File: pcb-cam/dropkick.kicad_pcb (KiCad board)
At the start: 2 copper layers, 44.5 x 50.8 mm, 55 parts, among them J1 Conn_01x10, SW1 450405020524, SW2 KMR211NG_LFS, U1 SPX3819-3.3, U2 MCP73831T-2ACI/OT, U3 CAM-M8C-0, U4 ATSAMD21G18A-AUT, U5 DPS310XTSA1, U6 MPU-6050, X1 USB micro-B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

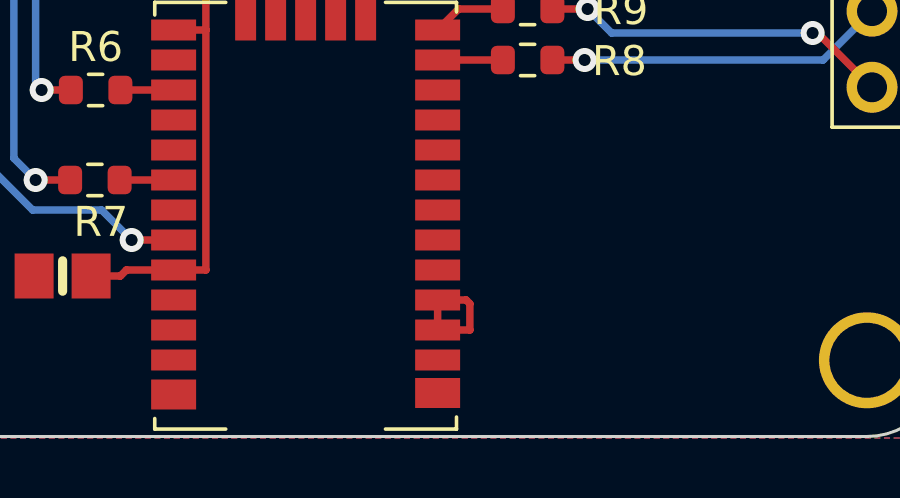
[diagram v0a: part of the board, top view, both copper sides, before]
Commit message: use internal antenna only
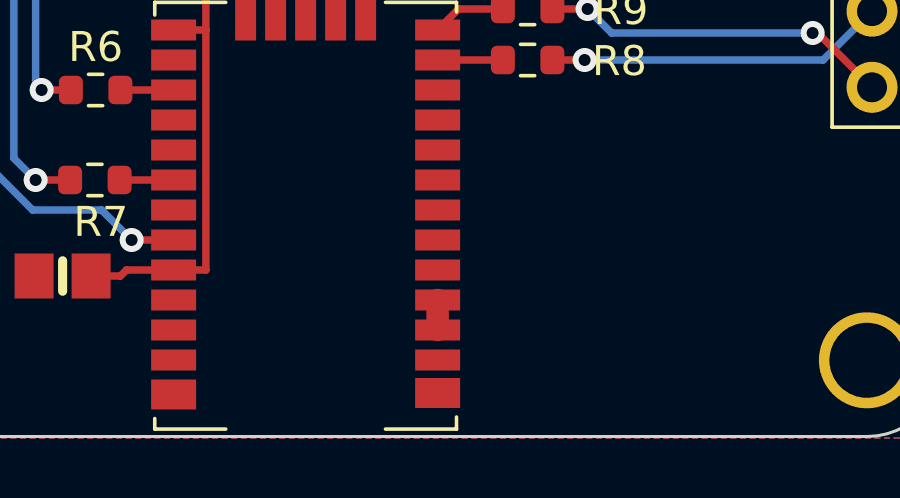
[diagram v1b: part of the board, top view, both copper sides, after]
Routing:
- net /RF: track 4.08 -> 1.00 mm
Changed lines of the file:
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@@
   (segment (start 93.275 81) (end 91.8 81) (width 0.25) (layer "F.Cu") (net 61))
   (segment (start 91.8 81) (end 91.1 81.7) (width 0.25) (layer "F.Cu") (net 61))
-  (segment (start 92.1753 90.8247) (end 92.050599 90.699999) (width 0.25) (layer "F.Cu") (net 74))
-  (segment (start 92.1753 91.7) (end 92.1753 90.8247) (width 0.25) (layer "F.Cu") (net 74))
-  (segment (start 91.1 91.7) (end 92.1753 91.7) (width 0.25) (layer "F.Cu") (net 74))
-  (segment (start 91.1 91.7) (end 91.1 90.699999) (width 0.25) (layer "F.Cu") (net 74))
-  (segment (start 92.050599 90.699999) (end 91.1 90.699999) (width 0.25) (layer "F.Cu") (net 74))
+  (segment (start 91.1 90.699999) (end 91.1 91.7) (width 0.75) (layer "F.Cu") (net 74))
   (zone (net 2) (net_name "GND") (layers F&B.Cu) (hatch edge 0.508)
     (connect_pads (clearance 0.508))

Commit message: V5-CAM PCB
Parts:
- removed H4: MountingHole, lib_fp:MOUNTINGHOLE_2.5_PLATED
- removed R8, R9: 20, Resistor_SMD:R_0603_1608Metric
- C1, C10, C11, C12, C13, C5, C7, C8: footprint lib_fp:0603-NO -> Capacitor_SMD:C_0603_1608Metric
- C2, C3, C4, C6, C9: footprint lib_fp:0805-NO -> Capacitor_SMD:C_0805_2012Metric
- CHG1, L1, L2: footprint lib_fp:CHIPLED_0805_NOOUTLINE -> LED_SMD:LED_0603_1608Metric
- L3: renamed from D2; footprint lib_fp:CHIPLED_0603_NOOUTLINE -> LED_SMD:LED_0603_1608Metric
- R1, R10, R11, R12, R15, R2, R3, R4, R5, SJ1: footprint lib_fp:0603-NO -> Resistor_SMD:R_0603_1608Metric
- R13, R14: footprint lib_fp:R_0603_1608Metric -> Resistor_SMD:R_0603_1608Metric
- R6, R7: footprint Resistor_SMD:R_0603_1608Metric -> Resistor_SMD:R_0402_1005Metric
- moved REF1 9.32 mm to (96.8, 85.1)
- moved R7 0.59 mm to (80.3, 86.7)
- moved R6 0.56 mm to (80.3, 83.7)
- moved C6 0.29 mm to (78.9, 89.8)
- turned CHG1 to 90 degrees
- turned L1 to -90 degrees
- turned L2 to -90 degrees
- turned L3 to 180 degrees
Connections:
- R10 pad 2: Net-(L2-PadA) -> Net-(L2-Pad2)
- R11 pad 1: Net-(L1-PadC) -> Net-(L1-Pad1)
- R12 pad 2: Net-(D2-PadA) -> Net-(L3-Pad2)
- R5 pad 1: Net-(CHG1-PadC) -> Net-(CHG1-Pad1)
- U3 pad 25: Net-(R8-Pad2) -> unconnected-(U3-Pad25)
- U3 pad 26: Net-(R9-Pad2) -> unconnected-(U3-Pad26)
- U6 pad THERM: GND -> (no net)
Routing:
- net Net-(CHG1-PadC): track 13.7 -> 0.00 mm
- net Net-(CHG1-Pad1): track 0.00 -> 13.7 mm
- net /D0: track 35.3 -> 24.0 mm, vias 2 -> 1
- net GND: track 218.1 -> 209.4 mm
- net Net-(L2-PadA): track 3.11 -> 0.00 mm
- net Net-(L2-Pad2): track 0.00 -> 3.11 mm
- net Net-(R9-Pad2): track 2.46 -> 0.00 mm
- net Net-(L3-Pad2): track 0.00 -> 2.20 mm
- net Net-(D2-PadA): track 2.20 -> 0.00 mm
- net Net-(R8-Pad2): track 2.18 -> 0.00 mm
- net Net-(L1-PadC): track 2.10 -> 0.00 mm
- net Net-(L1-Pad1): track 0.00 -> 2.10 mm
- net /SDA: track 70.3 -> 68.9 mm, vias 6 -> 4
- net +3V3: track 156.9 -> 155.9 mm, vias 5 -> 6
- net /D1: track 28.2 -> 27.4 mm, vias 3 -> 2
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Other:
- board text added: "Dropkick V5-CAM Copyright (c) 2022 Riley Rainey https://GitHub.com/rrainey/dropkick/"
- board text added: "Dropkick V5-CAM Riley Rainey"
- board text removed: "Dropkick V4 Copyright (c) 2022 Riley Rainey https://GitHub.com/rrainey/dropkick/"
- board text removed: "Dropkick V4 Riley Rainey"

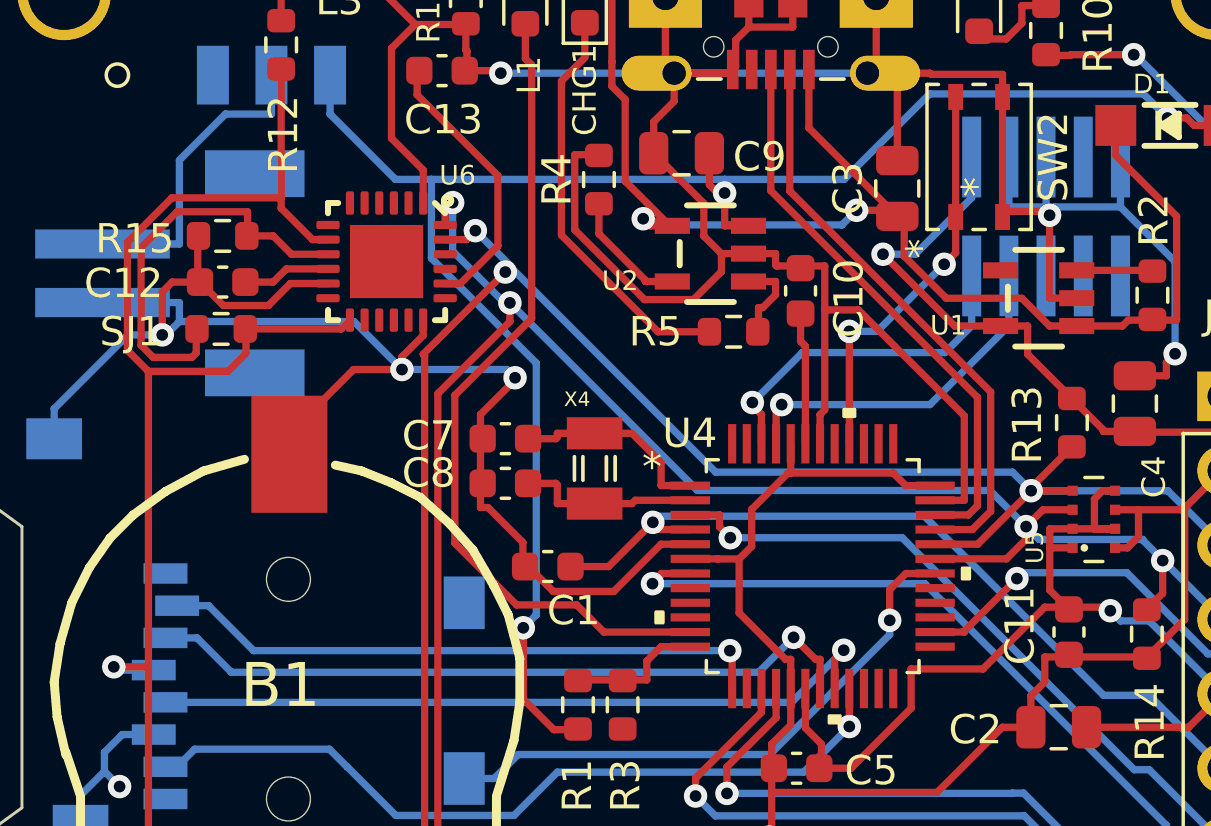
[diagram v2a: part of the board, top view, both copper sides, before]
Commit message: V5-CAM add INT line to MPU6050
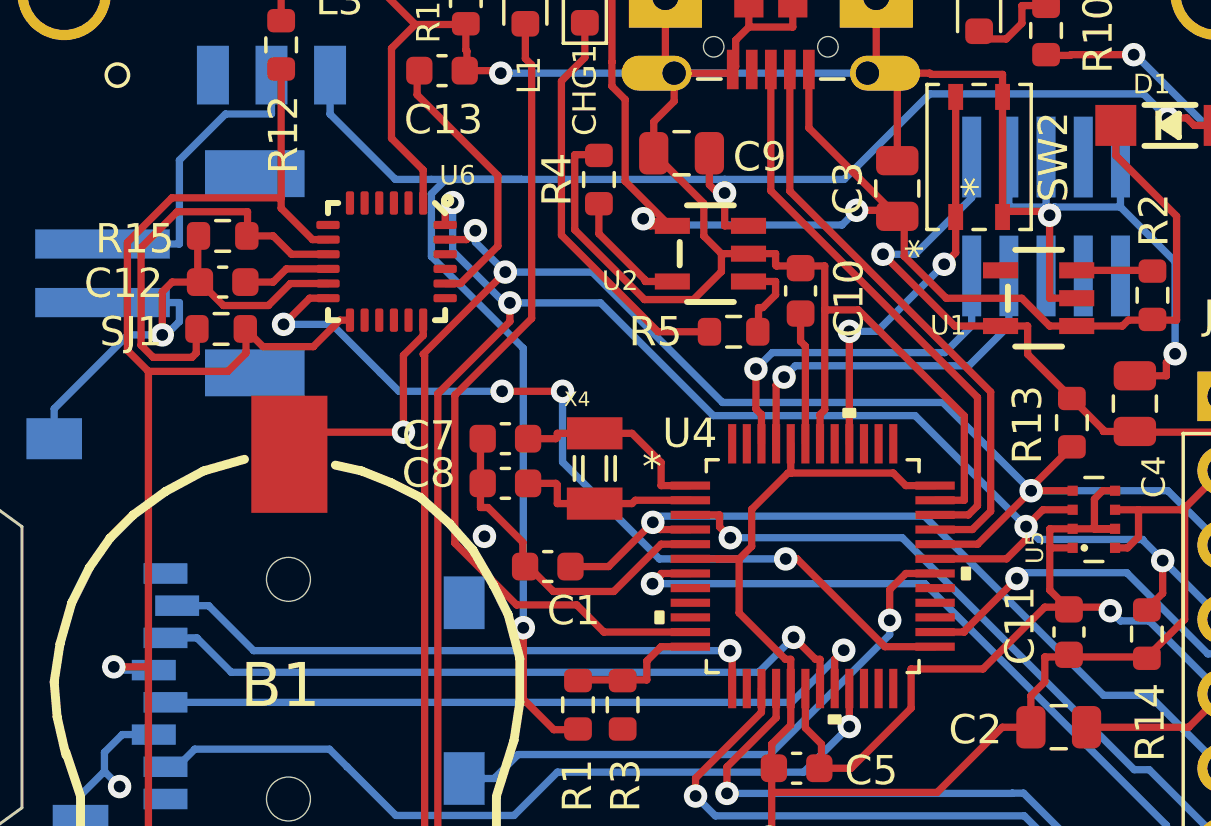
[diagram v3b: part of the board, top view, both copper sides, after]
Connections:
- U6 pad 12: /INT -> /D11
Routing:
- net /D11: track 0.00 -> 30.0 mm, vias 0 -> 4
- net GND: track 209.4 -> 195.9 mm
- net VBAT: track 69.5 -> 72.0 mm
- net +3V3: track 155.9 -> 156.5 mm
- net /SWCLK: track 12.0 -> 12.5 mm

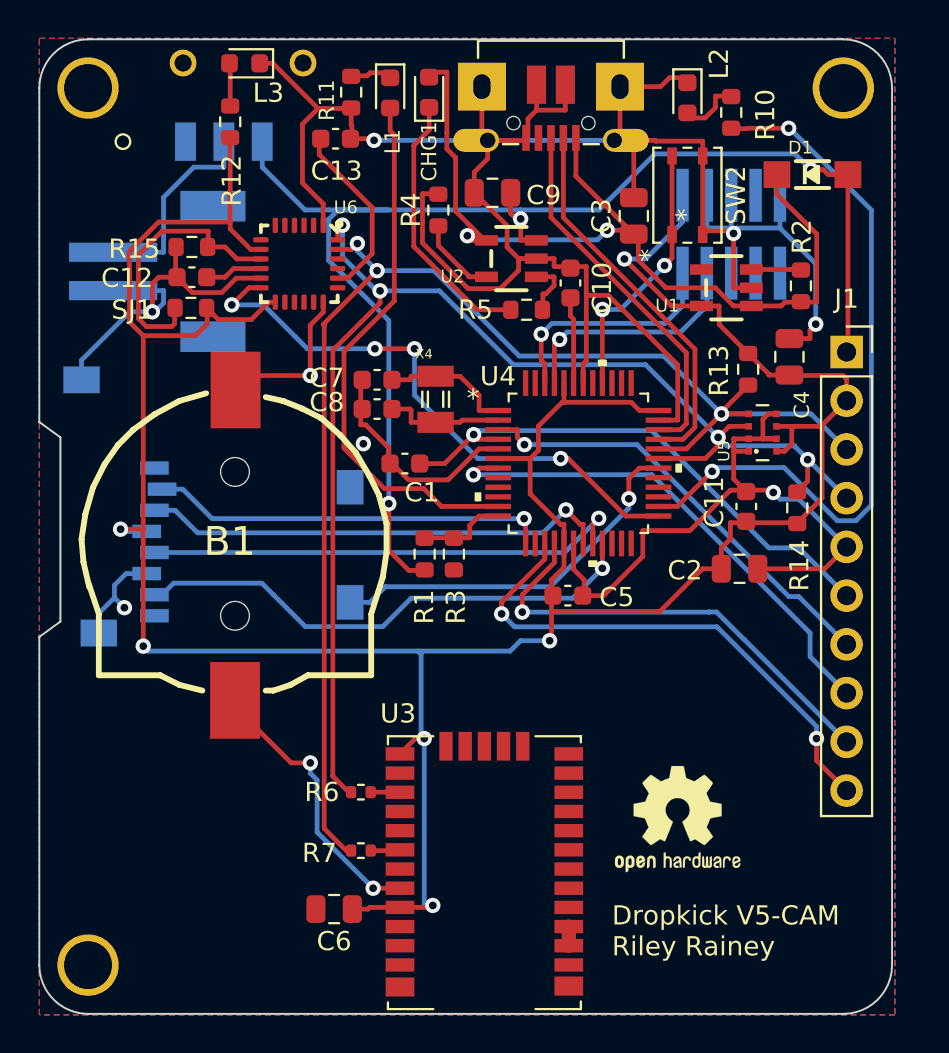
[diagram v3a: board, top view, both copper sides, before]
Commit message: Clean up AD0 address line for MPU6050
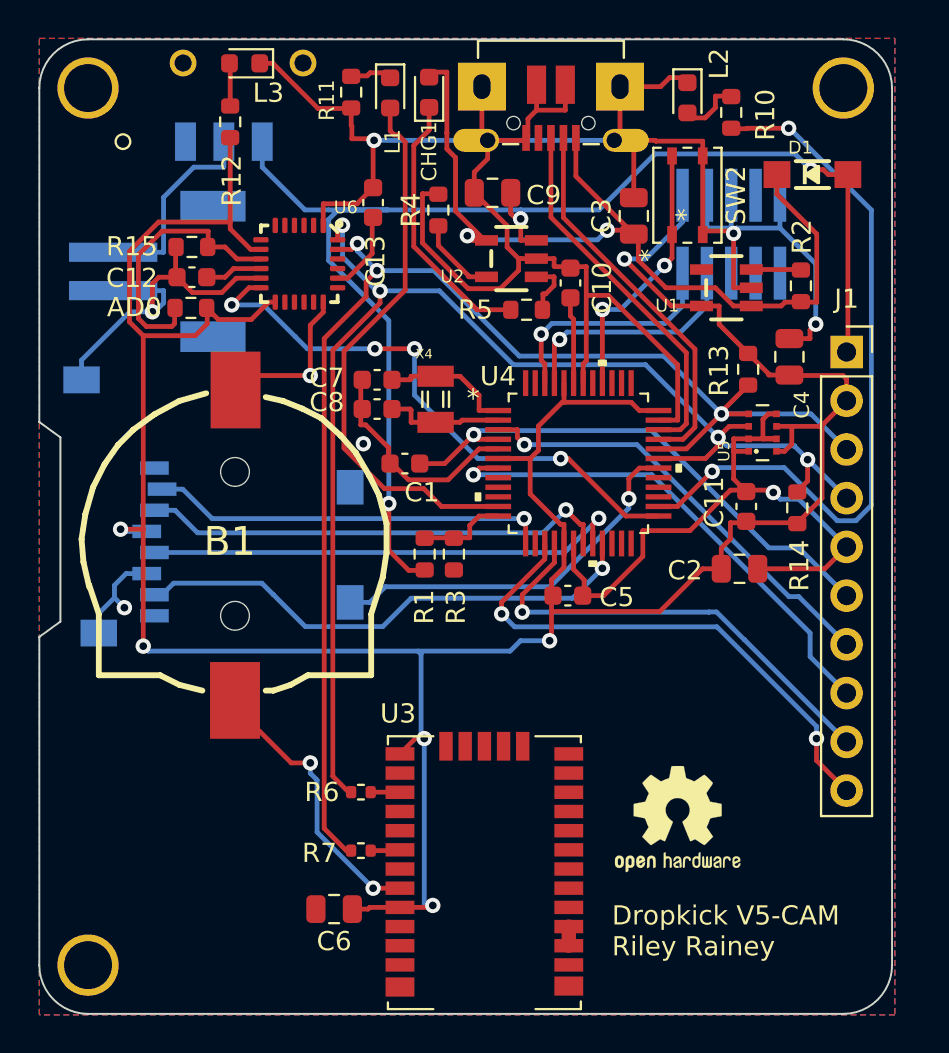
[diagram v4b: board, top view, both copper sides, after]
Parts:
- moved C13 3.86 mm to (80.9, 53.0), turned to 90 degrees
- renumbered SJ1 to AD0
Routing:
- net /CPOUT: track 9.46 -> 4.24 mm
- net /D8: track 27.9 -> 28.5 mm

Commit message: Improve LED wiring consistency; update gerber
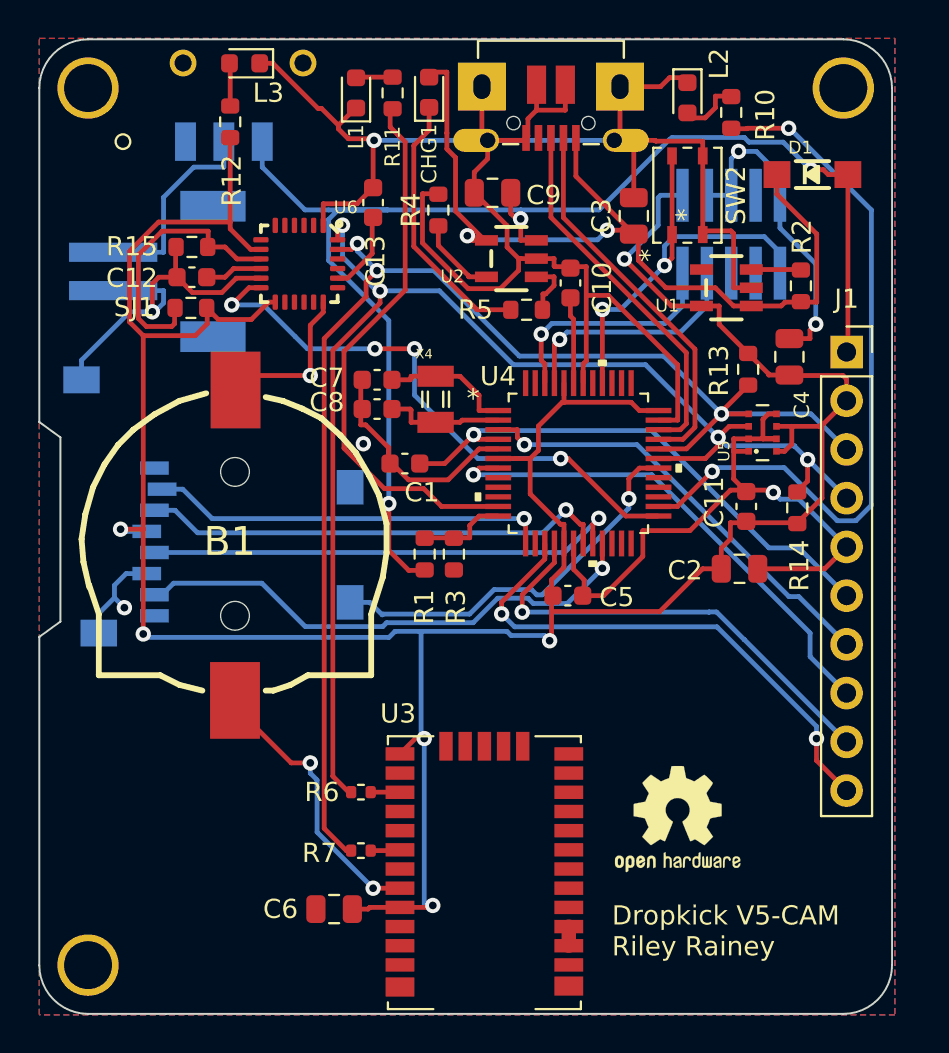
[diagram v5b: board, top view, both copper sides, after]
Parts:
- moved REF2 2.51 mm to (90.9, 71.0)
- moved R11 2.16 mm to (81.9, 47.2), turned to 90 degrees
- moved L1 1.78 mm to (80.0, 47.2), turned to 90 degrees
- renumbered AD0 to SJ1
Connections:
- JP1 pad 10: //RESET -> /~{RESET}
- L1 pad 1: Net-(L1-Pad1) -> GND
- L1 pad 2: /D8 -> Net-(L1-Pad2)
- R11 pad 1: Net-(L1-Pad1) -> /D8
- R11 pad 2: GND -> Net-(L1-Pad2)
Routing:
- net /~{RESET}: track 13.9 -> 22.6 mm
- net Net-(L1-Pad1): track 2.10 -> 0.00 mm
- net Net-(L1-Pad2): track 0.00 -> 1.92 mm
- net /D7: track 19.9 -> 20.6 mm
- net VBAT: track 72.0 -> 72.7 mm
- net +3V3: track 156.5 -> 157.0 mm
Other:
- board text added: "Dropkick V5-CAM Copyright (c) 2023 Riley Rainey https://GitHub.com/rrainey/dropkick/"
- board text removed: "Dropkick V5-CAM Copyright (c) 2022 Riley Rainey https://GitHub.com/rrainey/dropkick/"

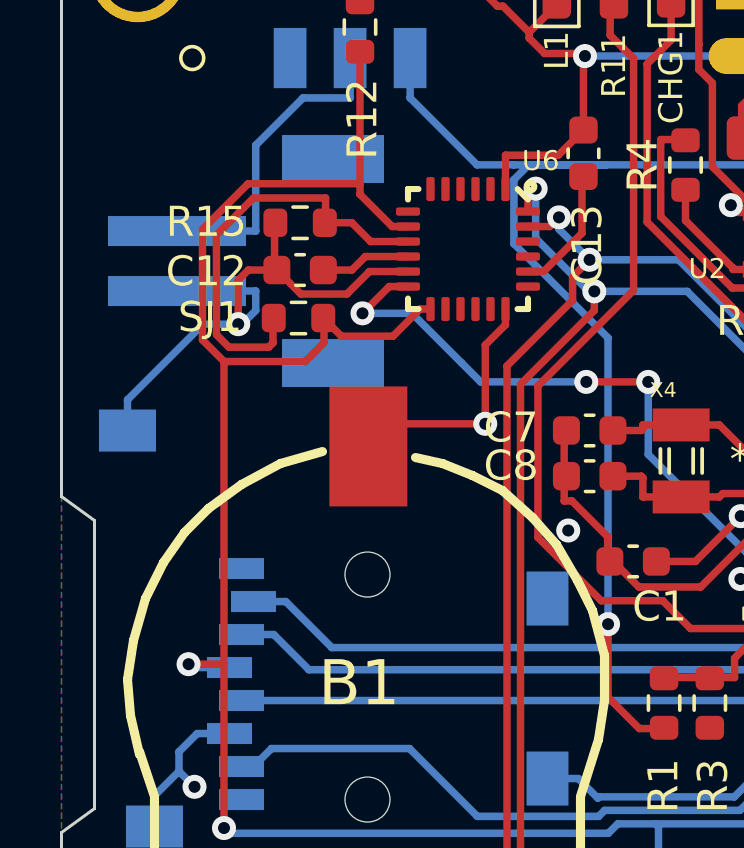
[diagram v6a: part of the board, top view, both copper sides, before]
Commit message: Add VLOGIC bypass cap to 6050; update gerbers
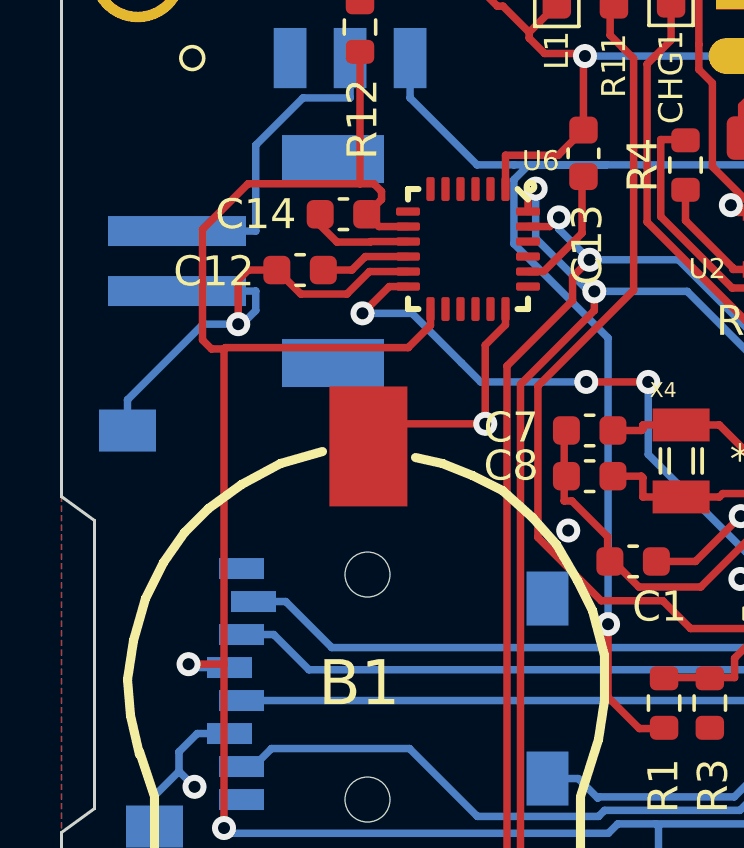
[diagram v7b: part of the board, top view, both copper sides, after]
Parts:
- removed R15: 10K, Resistor_SMD:R_0603_1608Metric
- removed SJ1: SOLDERJUMPER, Resistor_SMD:R_0603_1608Metric
- added C14: 10nF, Capacitor_SMD:C_0603_1608Metric, F.Cu at (72.9, 55.0)
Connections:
- U6 pad 9: /AD0 -> GND
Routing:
- net /AD0: track 14.2 -> 0.00 mm
- net GND: track 196.0 -> 197.9 mm

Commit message: Upgrade to KiCad 7
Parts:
- added C15: 0.1uF, Capacitor_SMD:C_0603_1608Metric, F.Cu at (76.2, 60.5)
- U6: footprint lib_fp:QFN24_4MM_SMSC -> lib_fp:MPU6XXX_QFN24_4MM_SMSC
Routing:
- net GND: track 197.9 -> 190.2 mm, vias 8 -> 9
- net +3V3: track 157.4 -> 158.5 mm
